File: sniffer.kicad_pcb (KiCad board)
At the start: 2 copper layers, 38.4 x 65.5 mm, 18 parts, among them J1 Conn_01x06, J2 PMSA003, Q1 Si2371EDS, Q2 Si2371EDS, U1 TTGO-T-Display

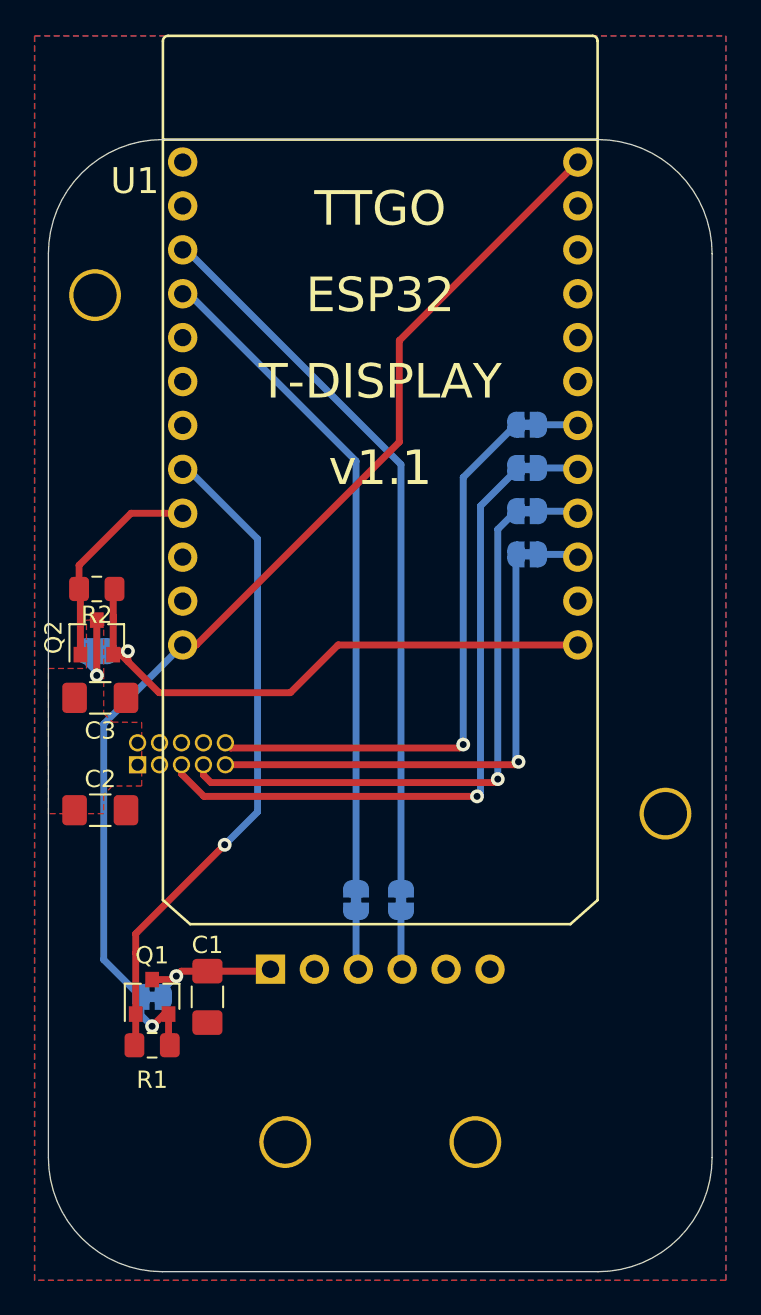
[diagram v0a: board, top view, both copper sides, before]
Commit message: sync: Miscellaneous tweaks
* Clean-up footprint mounting holes.
* Move some references.
* Add mounting holes to design.
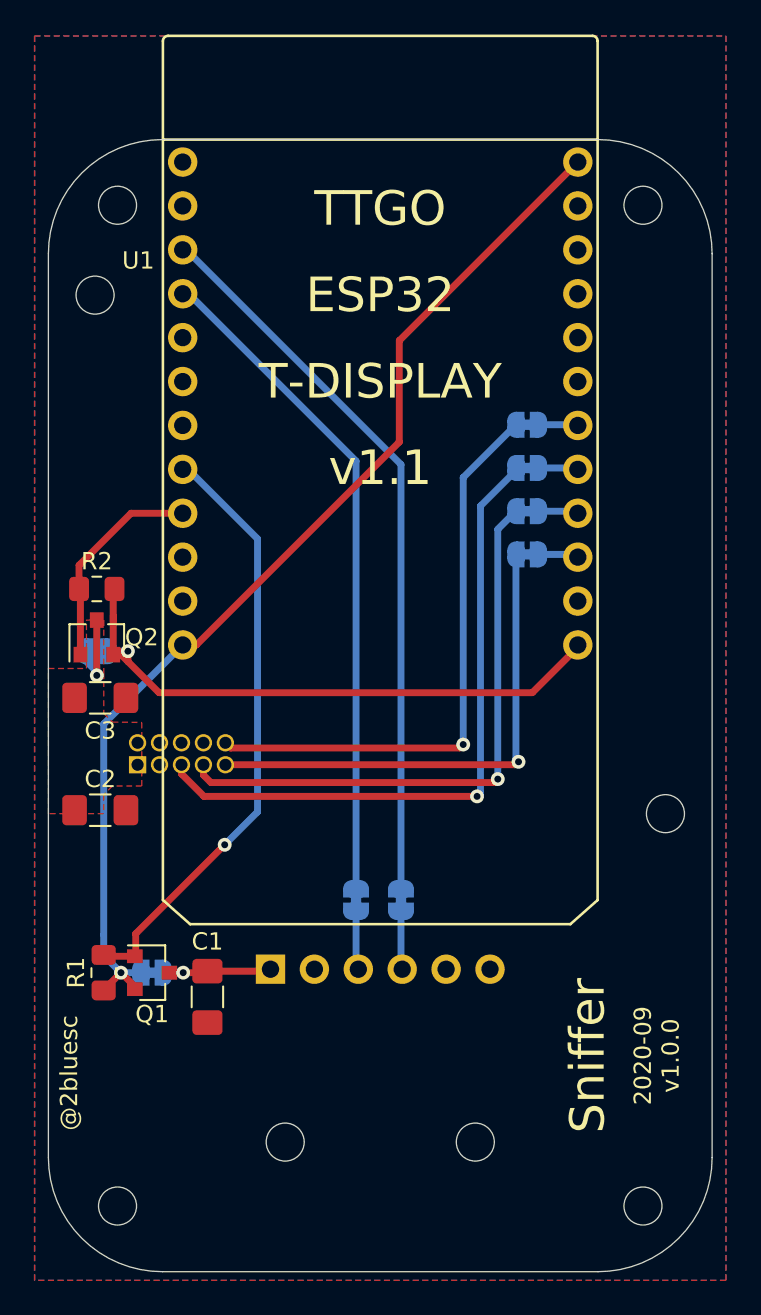
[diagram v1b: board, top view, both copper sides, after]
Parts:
- added H1: MountingHole, MountingHole:MountingHole_2.2mm_M2, F.Cu at (104.8, 39.8)
- added H2: MountingHole, MountingHole:MountingHole_2.2mm_M2, F.Cu at (104.8, 97.7)
- added H3: MountingHole, MountingHole:MountingHole_2.2mm_M2, F.Cu at (135.2, 39.8)
- added H4: MountingHole, MountingHole:MountingHole_2.2mm_M2, F.Cu at (135.2, 97.7)
- moved R1 5.05 mm to (104.0, 84.2), turned to 270 degrees
- moved JP1 1.40 mm to (106.8, 84.2)
- moved Q1 1.40 mm to (106.8, 84.2), turned to 0 degrees
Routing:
- net /BME_PWR: track 38.2 -> 34.7 mm
- net +3V3: track 66.1 -> 63.2 mm
- net Net-(C1-Pad1): track 8.61 -> 7.08 mm
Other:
- board text added: "2020-09 v1.0.0"
- board text added: "@2bluesc"
- board text added: "Sniffer"

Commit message: gerbers: First pass
* Looks plausible.
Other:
- board text added: "v1.0.0 2020-09 @2bluesc"
- board text removed: "2020-09 v1.0.0"
- board text removed: "@2bluesc"
